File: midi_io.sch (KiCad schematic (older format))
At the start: 6 parts

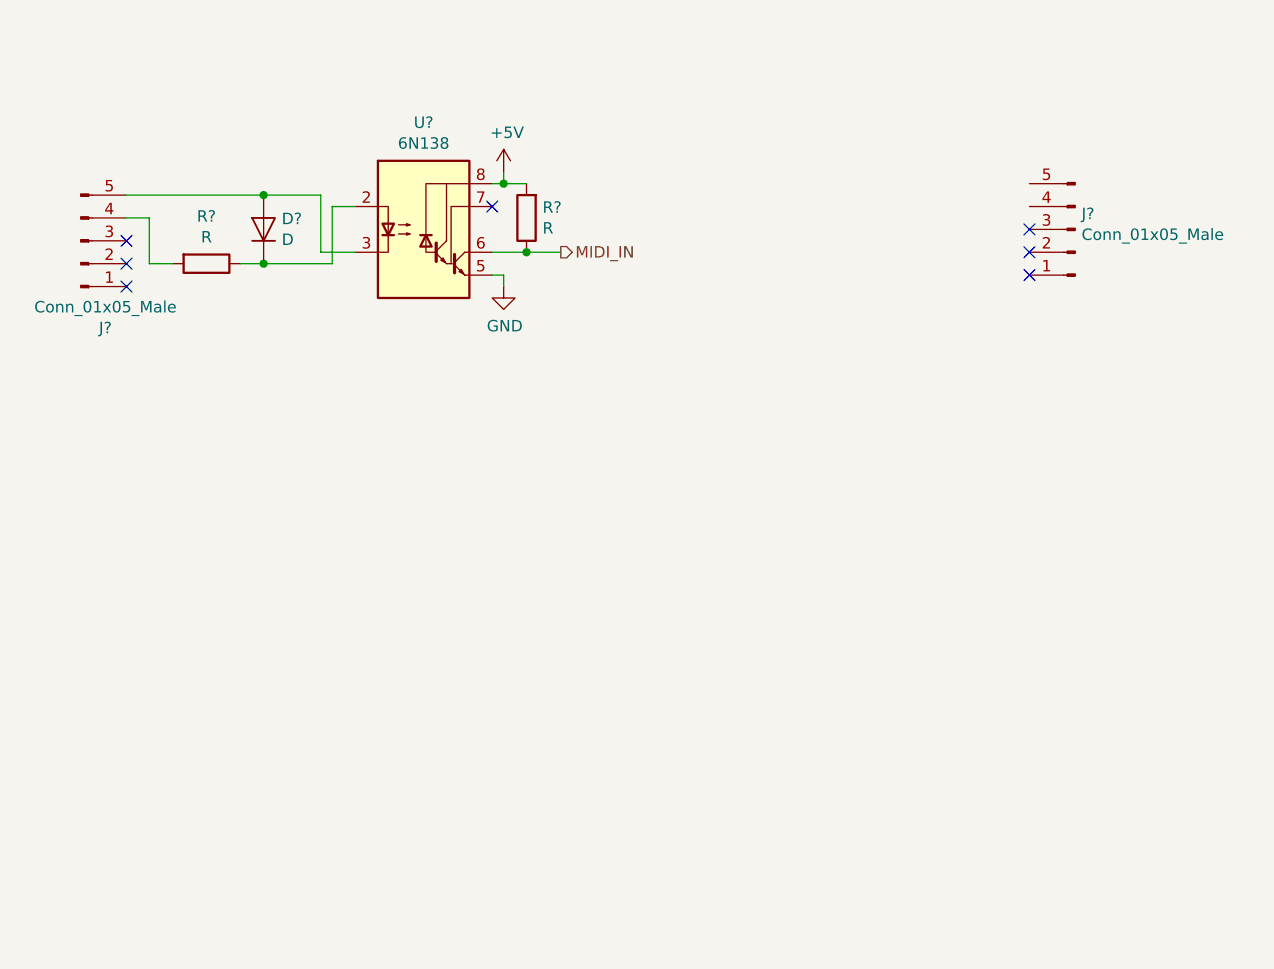
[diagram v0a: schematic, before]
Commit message: Schem entry done, need to do footprints and PCB
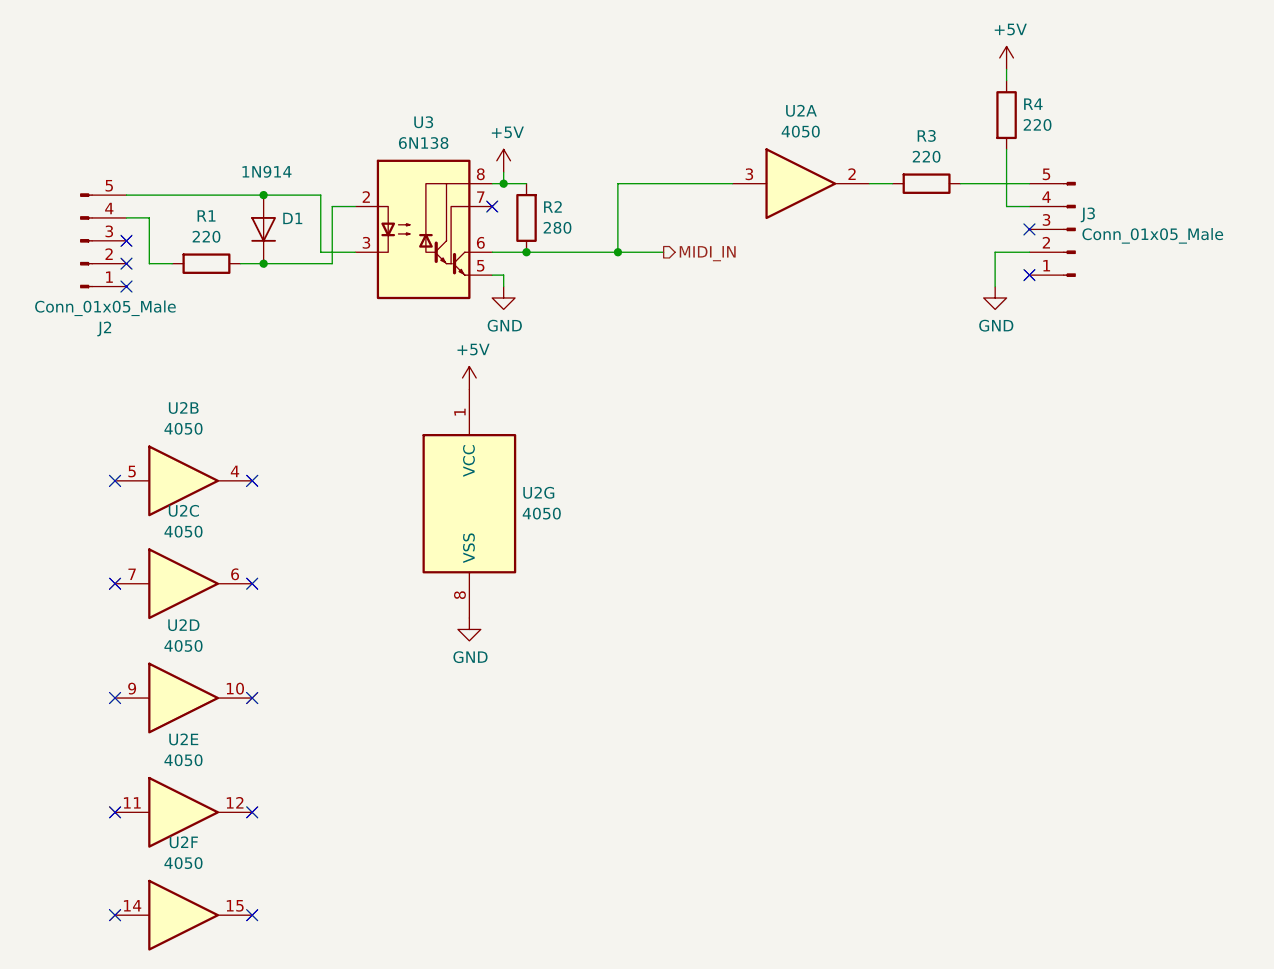
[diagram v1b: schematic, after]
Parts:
- added R3, R4: 220, symbol Device:R
- added U2: 4050, symbol 4xxx:4050
- D1: renamed from D?; value D -> 1N914
- R1: renamed from R?; value R -> 220
- R2: renamed from R?; value R -> 280
- gave numbers to parts that had none: 3
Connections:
- net +5V: now also R4.1, U2.1 (VCC)
- net GND: now also J3.2 (Pin_2), U2.8 (VSS)
- net MIDI_IN: now also U2.3
- net at J3.4 (Pin_4): now also R4.2
- net at J3.5 (Pin_5): now also R3.1
- new net: R3.2, U2.2
- no-connect marks 7 -> 16
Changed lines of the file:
@@
 EESchema Schematic File Version 4
 LIBS:midi_switcher-cache
-EELAYER 29 0
+EELAYER 30 0
 EELAYER END
 $Descr A4 11693 8268
@@
 $EndDescr
 $Comp
-L Connector:Conn_01x05_Male J?
+L Connector:Conn_01x05_Male J2
 U 1 1 5D75B250
 P 1750 1600
-F 0 "J?" H 1858 1981 50  0000 C CNN
+F 0 "J2" H 1858 1981 50  0000 C CNN
 F 1 "Conn_01x05_Male" H 1858 1890 50  0000 C CNN
 F 2 "" H 1750 1600 50  0001 C CNN
@@
 NoConn ~ 1950 1600
 $Comp
-L Device:D D?
+L Device:D D1
 U 1 1 5DBF71C3
 P 2550 1550
-F 0 "D?" V 2596 1471 50  0000 R CNN
-F 1 "D" V 2505 1471 50  0000 R CNN
+F 0 "D1" V 2596 1471 50  0000 R CNN
+F 1 "1N914" V 2800 1650 50  0000 R CNN
 F 2 "" H 2550 1550 50  0001 C CNN
 F 3 "~" H 2550 1550 50  0001 C CNN
@@
 $EndComp
 $Comp
-L Device:R R?
+L Device:R R1
 U 1 1 5DBF79C7
 P 2300 1700
-F 0 "R?" V 2093 1700 50  0000 C CNN
-F 1 "R" V 2184 1700 50  0000 C CNN
+F 0 "R1" V 2093 1700 50  0000 C CNN
+F 1 "220" V 2184 1700 50  0000 C CNN
 F 2 "" V 2230 1700 50  0001 C CNN
 F 3 "~" H 2300 1700 50  0001 C CNN
@@
 $EndComp
 $Comp
-L Isolator:6N138 U?
+L Isolator:6N138 U3
 U 1 1 5DBF8216
 P 3250 1550
-F 0 "U?" H 3250 2017 50  0000 C CNN
+F 0 "U3" H 3250 2017 50  0000 C CNN
 F 1 "6N138" H 3250 1926 50  0000 C CNN
 F 2 "" H 3540 1250 50  0001 C CNN
@@
 Connection ~ 2550 1700
 $Comp
-L power:+5V #PWR?
+L power:+5V #PWR0110
 U 1 1 5DBFC0C8
 P 3600 1300
-F 0 "#PWR?" H 3600 1150 50  0001 C CNN
+F 0 "#PWR0110" H 3600 1150 50  0001 C CNN
 F 1 "+5V" H 3615 1473 50  0000 C CNN
 F 2 "" H 3600 1300 50  0001 C CNN
@@
 NoConn ~ 3550 1450
 $Comp
-L power:GND #PWR?
+L power:GND #PWR0111
 U 1 1 5DBFCDB9
 P 3600 1800
-F 0 "#PWR?" H 3600 1550 50  0001 C CNN
+F 0 "#PWR0111" H 3600 1550 50  0001 C CNN
 F 1 "GND" H 3605 1627 50  0000 C CNN
 F 2 "" H 3600 1800 50  0001 C CNN
@@
 Connection ~ 3600 1350
 $Comp
-L Device:R R?
+L Device:R R2
 U 1 1 5DBFD43E
 P 3700 1500
-F 0 "R?" H 3630 1454 50  0000 R CNN
-F 1 "R" H 3630 1545 50  0000 R CNN
+F 0 "R2" H 3630 1454 50  0000 R CNN
+F 1 "280" H 3630 1545 50  0000 R CNN
 F 2 "" V 3630 1500 50  0001 C CNN
 F 3 "~" H 3700 1500 50  0001 C CNN
@@
 	3550 1650 3700 1650
 Connection ~ 3700 1650
-Wire Wire Line
-	3700 1650 3850 1650
-Text HLabel 3850 1650 2    50   Output ~ 0
+Text HLabel 4300 1650 2    50   Output ~ 0
 MIDI_IN
 NoConn ~ 5900 1550
-NoConn ~ 5900 1650
 NoConn ~ 5900 1750
 $Comp
-L Connector:Conn_01x05_Male J?
+L Connector:Conn_01x05_Male J3
 U 1 1 5D75D52C
 P 6100 1550
-F 0 "J?" H 6072 1482 50  0000 R CNN
+F 0 "J3" H 6072 1482 50  0000 R CNN
 F 1 "Conn_01x05_Male" H 6072 1573 50  0000 R CNN
 F 2 "" H 6100 1550 50  0001 C CNN
@@
 	-1   0    0    1
 $EndComp
+$Comp
+L 4xxx:4050 U2
+U 1 1 5DC4FB3B
+P 4900 1350
+F 0 "U2" H 4900 1667 50  0000 C CNN
+F 1 "4050" H 4900 1576 50  0000 C CNN
+F 2 "" H 4900 1350 50  0001 C CNN
+F 3 "http://www.intersil.com/content/dam/intersil/documents/cd40/cd4050bms.pdf" H 4900 1350 50  0001 C CNN
+	1    4900 1350
+	1    0    0    -1
+$EndComp
+$Comp
+L 4xxx:4050 U2
+U 2 1 5DC51768
+P 2200 2650
+F 0 "U2" H 2200 2967 50  0000 C CNN
+F 1 "4050" H 2200 2876 50  0000 C CNN
+F 2 "" H 2200 2650 50  0001 C CNN
+F 3 "http://www.intersil.com/content/dam/intersil/documents/cd40/cd4050bms.pdf" H 2200 2650 50  0001 C CNN
+	2    2200 2650
+	1    0    0    -1
+$EndComp
+$Comp
+L 4xxx:4050 U2
+U 3 1 5DC52771
+P 2200 3100
+F 0 "U2" H 2200 3417 50  0000 C CNN
+F 1 "4050" H 2200 3326 50  0000 C CNN
+F 2 "" H 2200 3100 50  0001 C CNN
+F 3 "http://www.intersil.com/content/dam/intersil/documents/cd40/cd4050bms.pdf" H 2200 3100 50  0001 C CNN
+	3    2200 3100
+	1    0    0    -1
+$EndComp
+$Comp
+L 4xxx:4050 U2
+U 4 1 5DC54BC7
+P 2200 3600
+F 0 "U2" H 2200 3917 50  0000 C CNN
+F 1 "4050" H 2200 3826 50  0000 C CNN
+F 2 "" H 2200 3600 50  0001 C CNN
+F 3 "http://www.intersil.com/content/dam/intersil/documents/cd40/cd4050bms.pdf" H 2200 3600 50  0001 C CNN
+	4    2200 3600
+	1    0    0    -1
+$EndComp
+$Comp
+L 4xxx:4050 U2
+U 5 1 5DC55CCF
+P 2200 4100
+F 0 "U2" H 2200 4417 50  0000 C CNN
+F 1 "4050" H 2200 4326 50  0000 C CNN
+F 2 "" H 2200 4100 50  0001 C CNN
+F 3 "http://www.intersil.com/content/dam/intersil/documents/cd40/cd4050bms.pdf" H 2200 4100 50  0001 C CNN
+	5    2200 4100
+	1    0    0    -1
+$EndComp
+$Comp
+L 4xxx:4050 U2
+U 6 1 5DC5829B
+P 2200 4550
+F 0 "U2" H 2200 4867 50  0000 C CNN
+F 1 "4050" H 2200 4776 50  0000 C CNN
+F 2 "" H 2200 4550 50  0001 C CNN
+F 3 "http://www.intersil.com/content/dam/intersil/documents/cd40/cd4050bms.pdf" H 2200 4550 50  0001 C CNN
+	6    2200 4550
+	1    0    0    -1
+$EndComp
+$Comp
+L 4xxx:4050 U2
+U 7 1 5DC5970D
+P 3450 2750
+F 0 "U2" H 3680 2796 50  0000 L CNN
+F 1 "4050" H 3680 2705 50  0000 L CNN
+F 2 "" H 3450 2750 50  0001 C CNN
+F 3 "http://www.intersil.com/content/dam/intersil/documents/cd40/cd4050bms.pdf" H 3450 2750 50  0001 C CNN
+	7    3450 2750
+	1    0    0    -1
+$EndComp
+NoConn ~ 1900 2650
+NoConn ~ 2500 2650
+NoConn ~ 1900 3100
+NoConn ~ 2500 3100
+NoConn ~ 1900 3600
+NoConn ~ 2500 3600
+NoConn ~ 1900 4100
+NoConn ~ 2500 4100
+NoConn ~ 1900 4550
+NoConn ~ 2500 4550
+$Comp
+L power:+5V #PWR0112
+U 1 1 5DC6299F
+P 3450 2250
+F 0 "#PWR0112" H 3450 2100 50  0001 C CNN
+F 1 "+5V" H 3465 2423 50  0000 C CNN
+F 2 "" H 3450 2250 50  0001 C CNN
+F 3 "" H 3450 2250 50  0001 C CNN
+	1    3450 2250
+	1    0    0    -1
+$EndComp
+$Comp
+L power:GND #PWR0113
+U 1 1 5DC63183
+P 3450 3250
+F 0 "#PWR0113" H 3450 3000 50  0001 C CNN
+F 1 "GND" H 3455 3077 50  0000 C CNN
+F 2 "" H 3450 3250 50  0001 C CNN
+F 3 "" H 3450 3250 50  0001 C CNN
+	1    3450 3250
+	1    0    0    -1
+$EndComp
+$Comp
+L Device:R R3
+U 1 1 5DC6727B
+P 5450 1350
+F 0 "R3" V 5243 1350 50  0000 C CNN
+F 1 "220" V 5334 1350 50  0000 C CNN
+F 2 "" V 5380 1350 50  0001 C CNN
+F 3 "~" H 5450 1350 50  0001 C CNN
+	1    5450 1350
+	0    1    1    0
+$EndComp
+$Comp
+L power:GND #PWR0114
+U 1 1 5DC69599
+P 5750 1800
+F 0 "#PWR0114" H 5750 1550 50  0001 C CNN
+F 1 "GND" H 5755 1627 50  0000 C CNN
+F 2 "" H 5750 1800 50  0001 C CNN
+F 3 "" H 5750 1800 50  0001 C CNN
+	1    5750 1800
+	1    0    0    -1
+$EndComp
+Wire Wire Line
+	5750 1800 5750 1650
+Wire Wire Line
+	5750 1650 5900 1650
+Wire Wire Line
+	5200 1350 5300 1350
+Wire Wire Line
+	5600 1350 5900 1350
+$Comp
+L power:+5V #PWR0115
+U 1 1 5DC6A9F9
+P 5800 850
+F 0 "#PWR0115" H 5800 700 50  0001 C CNN
+F 1 "+5V" H 5815 1023 50  0000 C CNN
+F 2 "" H 5800 850 50  0001 C CNN
+F 3 "" H 5800 850 50  0001 C CNN
+	1    5800 850
+	1    0    0    -1
+$EndComp
+$Comp
+L Device:R R4
+U 1 1 5DC6B173
+P 5800 1050
+F 0 "R4" H 5870 1096 50  0000 L CNN
+F 1 "220" H 5870 1005 50  0000 L CNN
+F 2 "" V 5730 1050 50  0001 C CNN
+F 3 "~" H 5800 1050 50  0001 C CNN
+	1    5800 1050
+	1    0    0    -1
+$EndComp
+Wire Wire Line
+	5800 850  5800 900
+Wire Wire Line
+	5800 1200 5800 1450
+Wire Wire Line
+	5800 1450 5900 1450
+Wire Wire Line
+	3700 1650 4100 1650
+Wire Wire Line
+	4600 1350 4100 1350
+Wire Wire Line
+	4100 1350 4100 1650
+Connection ~ 4100 1650
+Wire Wire Line
+	4100 1650 4300 1650
 $EndSCHEMATC

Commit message: pushing for work to do over holiday
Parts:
- removed U2: 4050, symbol 4xxx:4050
- added U2: 74HC7014, Package_SO:SOIC-14_3.9x8.7mm_P1.27mm, symbol 74xx:74HC7014
- D1: footprint (none) -> Diode_THT:D_DO-35_SOD27_P10.16mm_Horizontal
- J2, J3: footprint (none) -> TerminalBlock:TerminalBlock_bornier-5_P5.08mm
- R1, R2, R3, R4: footprint (none) -> Resistor_THT:R_Axial_DIN0207_L6.3mm_D2.5mm_P10.16mm_Horizontal
- U3: footprint (none) -> Package_DIP:DIP-8_W10.16mm
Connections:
- net +5V: now also U2.14 (VCC)
- net GND: now also U2.7 (GND)
- net MIDI_IN: now also U2.1
- net at R3.2: now also U2.2
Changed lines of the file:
@@
 EESchema Schematic File Version 4
 LIBS:midi_switcher-cache
-EELAYER 30 0
+EELAYER 29 0
 EELAYER END
 $Descr A4 11693 8268
@@
 F 0 "J2" H 1858 1981 50  0000 C CNN
 F 1 "Conn_01x05_Male" H 1858 1890 50  0000 C CNN
-F 2 "" H 1750 1600 50  0001 C CNN
+F 2 "TerminalBlock:TerminalBlock_bornier-5_P5.08mm" H 1750 1600 50  0001 C CNN
 F 3 "~" H 1750 1600 50  0001 C CNN
 	1    1750 1600
@@
 F 0 "D1" V 2596 1471 50  0000 R CNN
 F 1 "1N914" V 2800 1650 50  0000 R CNN
-F 2 "" H 2550 1550 50  0001 C CNN
+F 2 "Diode_THT:D_DO-35_SOD27_P10.16mm_Horizontal" H 2550 1550 50  0001 C CNN
 F 3 "~" H 2550 1550 50  0001 C CNN
 	1    2550 1550
@@
 F 0 "R1" V 2093 1700 50  0000 C CNN
 F 1 "220" V 2184 1700 50  0000 C CNN
-F 2 "" V 2230 1700 50  0001 C CNN
+F 2 "Resistor_THT:R_Axial_DIN0207_L6.3mm_D2.5mm_P10.16mm_Horizontal" V 2230 1700 50  0001 C CNN
 F 3 "~" H 2300 1700 50  0001 C CNN
 	1    2300 1700
@@
 F 0 "U3" H 3250 2017 50  0000 C CNN
 F 1 "6N138" H 3250 1926 50  0000 C CNN
-F 2 "" H 3540 1250 50  0001 C CNN
+F 2 "Package_DIP:DIP-8_W10.16mm" H 3540 1250 50  0001 C CNN
 F 3 "http://www.onsemi.com/pub/Collateral/HCPL2731-D.pdf" H 3540 1250 50  0001 C CNN
 	1    3250 1550
@@
 F 0 "R2" H 3630 1454 50  0000 R CNN
 F 1 "280" H 3630 1545 50  0000 R CNN
-F 2 "" V 3630 1500 50  0001 C CNN
+F 2 "Resistor_THT:R_Axial_DIN0207_L6.3mm_D2.5mm_P10.16mm_Horizontal" V 3630 1500 50  0001 C CNN
 F 3 "~" H 3700 1500 50  0001 C CNN
 	1    3700 1500
@@
 F 0 "J3" H 6072 1482 50  0000 R CNN
 F 1 "Conn_01x05_Male" H 6072 1573 50  0000 R CNN
-F 2 "" H 6100 1550 50  0001 C CNN
+F 2 "TerminalBlock:TerminalBlock_bornier-5_P5.08mm" H 6100 1550 50  0001 C CNN
 F 3 "~" H 6100 1550 50  0001 C CNN
 	1    6100 1550
 	-1   0    0    1
 $EndComp
-$Comp
-L 4xxx:4050 U2
-U 1 1 5DC4FB3B
-P 4900 1350
-F 0 "U2" H 4900 1667 50  0000 C CNN
-F 1 "4050" H 4900 1576 50  0000 C CNN
-F 2 "" H 4900 1350 50  0001 C CNN
-F 3 "http://www.intersil.com/content/dam/intersil/documents/cd40/cd4050bms.pdf" H 4900 1350 50  0001 C CNN
-	1    4900 1350
-	1    0    0    -1
-$EndComp
-$Comp
-L 4xxx:4050 U2
-U 2 1 5DC51768
-P 2200 2650
-F 0 "U2" H 2200 2967 50  0000 C CNN
-F 1 "4050" H 2200 2876 50  0000 C CNN
-F 2 "" H 2200 2650 50  0001 C CNN
-F 3 "http://www.intersil.com/content/dam/intersil/documents/cd40/cd4050bms.pdf" H 2200 2650 50  0001 C CNN
-	2    2200 2650
-	1    0    0    -1
-$EndComp
-$Comp
-L 4xxx:4050 U2
-U 3 1 5DC52771
-P 2200 3100
-F 0 "U2" H 2200 3417 50  0000 C CNN
-F 1 "4050" H 2200 3326 50  0000 C CNN
-F 2 "" H 2200 3100 50  0001 C CNN
-F 3 "http://www.intersil.com/content/dam/intersil/documents/cd40/cd4050bms.pdf" H 2200 3100 50  0001 C CNN
-	3    2200 3100
-	1    0    0    -1
-$EndComp
-$Comp
-L 4xxx:4050 U2
-U 4 1 5DC54BC7
-P 2200 3600
-F 0 "U2" H 2200 3917 50  0000 C CNN
-F 1 "4050" H 2200 3826 50  0000 C CNN
-F 2 "" H 2200 3600 50  0001 C CNN
-F 3 "http://www.intersil.com/content/dam/intersil/documents/cd40/cd4050bms.pdf" H 2200 3600 50  0001 C CNN
-	4    2200 3600
-	1    0    0    -1
-$EndComp
-$Comp
-L 4xxx:4050 U2
-U 5 1 5DC55CCF
-P 2200 4100
-F 0 "U2" H 2200 4417 50  0000 C CNN
-F 1 "4050" H 2200 4326 50  0000 C CNN
-F 2 "" H 2200 4100 50  0001 C CNN
-F 3 "http://www.intersil.com/content/dam/intersil/documents/cd40/cd4050bms.pdf" H 2200 4100 50  0001 C CNN
-	5    2200 4100
-	1    0    0    -1
-$EndComp
-$Comp
-L 4xxx:4050 U2
-U 6 1 5DC5829B
-P 2200 4550
-F 0 "U2" H 2200 4867 50  0000 C CNN
-F 1 "4050" H 2200 4776 50  0000 C CNN
-F 2 "" H 2200 4550 50  0001 C CNN
-F 3 "http://www.intersil.com/content/dam/intersil/documents/cd40/cd4050bms.pdf" H 2200 4550 50  0001 C CNN
-	6    2200 4550
-	1    0    0    -1
-$EndComp
-$Comp
-L 4xxx:4050 U2
-U 7 1 5DC5970D
-P 3450 2750
-F 0 "U2" H 3680 2796 50  0000 L CNN
-F 1 "4050" H 3680 2705 50  0000 L CNN
-F 2 "" H 3450 2750 50  0001 C CNN
-F 3 "http://www.intersil.com/content/dam/intersil/documents/cd40/cd4050bms.pdf" H 3450 2750 50  0001 C CNN
-	7    3450 2750
-	1    0    0    -1
-$EndComp
-NoConn ~ 1900 2650
-NoConn ~ 2500 2650
-NoConn ~ 1900 3100
-NoConn ~ 2500 3100
-NoConn ~ 1900 3600
-NoConn ~ 2500 3600
-NoConn ~ 1900 4100
-NoConn ~ 2500 4100
-NoConn ~ 1900 4550
-NoConn ~ 2500 4550
 $Comp
 L power:+5V #PWR0112
@@
 $EndComp
 $Comp
-L power:GND #PWR0113
-U 1 1 5DC63183
-P 3450 3250
-F 0 "#PWR0113" H 3450 3000 50  0001 C CNN
-F 1 "GND" H 3455 3077 50  0000 C CNN
-F 2 "" H 3450 3250 50  0001 C CNN
-F 3 "" H 3450 3250 50  0001 C CNN
-	1    3450 3250
-	1    0    0    -1
-$EndComp
-$Comp
 L Device:R R3
 U 1 1 5DC6727B
@@
 F 0 "R3" V 5243 1350 50  0000 C CNN
 F 1 "220" V 5334 1350 50  0000 C CNN
-F 2 "" V 5380 1350 50  0001 C CNN
+F 2 "Resistor_THT:R_Axial_DIN0207_L6.3mm_D2.5mm_P10.16mm_Horizontal" V 5380 1350 50  0001 C CNN
 F 3 "~" H 5450 1350 50  0001 C CNN
 	1    5450 1350
@@
 F 0 "R4" H 5870 1096 50  0000 L CNN
 F 1 "220" H 5870 1005 50  0000 L CNN
-F 2 "" V 5730 1050 50  0001 C CNN
+F 2 "Resistor_THT:R_Axial_DIN0207_L6.3mm_D2.5mm_P10.16mm_Horizontal" V 5730 1050 50  0001 C CNN
 F 3 "~" H 5800 1050 50  0001 C CNN
 	1    5800 1050
@@
 Wire Wire Line
 	4100 1650 4300 1650
+$Comp
+L 74xx:74HC7014 U2
+U 1 1 5DC8D313
+P 4900 1350
+F 0 "U2" H 4900 1667 50  0000 C CNN
+F 1 "74HC7014" H 4900 1576 50  0000 C CNN
+F 2 "Package_SO:SOIC-14_3.9x8.7mm_P1.27mm" H 4900 1350 50  0001 C CNN
+F 3 "https://assets.nexperia.com/documents/data-sheet/74HC7014.pdf" H 4900 1350 50  0001 C CNN
+	1    4900 1350
+	1    0    0    -1
+$EndComp
+$Comp
+L 74xx:74HC7014 U2
+U 2 1 5DC91066
+P 1900 2550
+F 0 "U2" H 1900 2867 50  0000 C CNN
+F 1 "74HC7014" H 1900 2776 50  0000 C CNN
+F 2 "Package_SO:SOIC-14_3.9x8.7mm_P1.27mm" H 1900 2550 50  0001 C CNN
+F 3 "https://assets.nexperia.com/documents/data-sheet/74HC7014.pdf" H 1900 2550 50  0001 C CNN
+	2    1900 2550
+	1    0    0    -1
+$EndComp
+$Comp
+L 74xx:74HC7014 U2
+U 3 1 5DC92352
+P 1900 3050
+F 0 "U2" H 1900 3367 50  0000 C CNN
+F 1 "74HC7014" H 1900 3276 50  0000 C CNN
+F 2 "Package_SO:SOIC-14_3.9x8.7mm_P1.27mm" H 1900 3050 50  0001 C CNN
+F 3 "https://assets.nexperia.com/documents/data-sheet/74HC7014.pdf" H 1900 3050 50  0001 C CNN
+	3    1900 3050
+	1    0    0    -1
+$EndComp
+$Comp
+L 74xx:74HC7014 U2
+U 4 1 5DC946B7
+P 1900 3550
+F 0 "U2" H 1900 3867 50  0000 C CNN
+F 1 "74HC7014" H 1900 3776 50  0000 C CNN
+F 2 "Package_SO:SOIC-14_3.9x8.7mm_P1.27mm" H 1900 3550 50  0001 C CNN
+F 3 "https://assets.nexperia.com/documents/data-sheet/74HC7014.pdf" H 1900 3550 50  0001 C CNN
+	4    1900 3550
+	1    0    0    -1
+$EndComp
+$Comp
+L 74xx:74HC7014 U2
+U 5 1 5DC96433
+P 1900 4050
+F 0 "U2" H 1900 4367 50  0000 C CNN
+F 1 "74HC7014" H 1900 4276 50  0000 C CNN
+F 2 "Package_SO:SOIC-14_3.9x8.7mm_P1.27mm" H 1900 4050 50  0001 C CNN
+F 3 "https://assets.nexperia.com/documents/data-sheet/74HC7014.pdf" H 1900 4050 50  0001 C CNN
+	5    1900 4050
+	1    0    0    -1
+$EndComp
+$Comp
+L 74xx:74HC7014 U2
+U 6 1 5DC987BF
+P 1950 4500
+F 0 "U2" H 1950 4817 50  0000 C CNN
+F 1 "74HC7014" H 1950 4726 50  0000 C CNN
+F 2 "Package_SO:SOIC-14_3.9x8.7mm_P1.27mm" H 1950 4500 50  0001 C CNN
+F 3 "https://assets.nexperia.com/documents/data-sheet/74HC7014.pdf" H 1950 4500 50  0001 C CNN
+	6    1950 4500
+	1    0    0    -1
+$EndComp
+$Comp
+L 74xx:74HC7014 U2
+U 7 1 5DC9A07A
+P 3450 2750
+F 0 "U2" H 3680 2796 50  0000 L CNN
+F 1 "74HC7014" H 3680 2705 50  0000 L CNN
+F 2 "Package_SO:SOIC-14_3.9x8.7mm_P1.27mm" H 3450 2750 50  0001 C CNN
+F 3 "https://assets.nexperia.com/documents/data-sheet/74HC7014.pdf" H 3450 2750 50  0001 C CNN
+	7    3450 2750
+	1    0    0    -1
+$EndComp
+$Comp
+L power:GND #PWR01
+U 1 1 5DC9C5C7
+P 3450 3250
+F 0 "#PWR01" H 3450 3000 50  0001 C CNN
+F 1 "GND" H 3455 3077 50  0000 C CNN
+F 2 "" H 3450 3250 50  0001 C CNN
+F 3 "" H 3450 3250 50  0001 C CNN
+	1    3450 3250
+	1    0    0    -1
+$EndComp
+NoConn ~ 1600 2550
+NoConn ~ 2200 2550
+NoConn ~ 2200 3050
+NoConn ~ 1600 3050
+NoConn ~ 1600 3550
+NoConn ~ 2200 3550
+NoConn ~ 2200 4050
+NoConn ~ 1600 4050
+NoConn ~ 1650 4500
+NoConn ~ 2250 4500
 $EndSCHEMATC
